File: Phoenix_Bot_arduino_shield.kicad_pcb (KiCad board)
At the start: 2 copper layers, 135.9 x 64.8 mm, 41 parts, among them J1 Analog_signal_male, J14 PWN(10-5), J15 On Board Supply, J16 1x8 Male, J17 1x8 Male, J18 PWM_(6-1), J19 Analog_Pin_1, J2 Encoder_Signal, J20 1x8 Female, J21 1x8 Female, J22 Serial, J23 ICSP, J24 Analog_Pin_2, J25 Digital_Pins, J27 Solenoid_terminal, J28 Solendoid_middle_terminal, J29 bottom_solenoid_terminal, J3 Servo_signal, J4 Analog_signal_female, J5 encoder_power, J6 Servo_ground, J7 encoder_ground, J8 12V_terminal, q1 solenoid_1, q2 solenoid_4, q3 solenoid_3, q4 solenoid_5, q5 solenoid_3, q6 solenoid_6

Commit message: Board design finished. Final review needed.
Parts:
- added G***: LOGO, ARC:arc-silk, F.Cu at (137.2, 105.4)
- added REF**: via-0.7mm, footprints:via-0.7mm, F.Cu at (245.1, 66.0)
- added REF**: via-0.7mm, footprints:via-0.7mm, F.Cu at (245.1, 123.8)
- added REF**: via-0.7mm, footprints:via-0.7mm, F.Cu at (236.2, 78.1)
- added REF**: via-0.7mm, footprints:via-0.7mm, F.Cu at (234.9, 78.1)
- added REF**: via-0.7mm, footprints:via-0.7mm, F.Cu at (246.4, 67.9)
- added REF**: via-0.7mm, footprints:via-0.7mm, F.Cu at (245.1, 67.9)
- added REF**: via-0.7mm, footprints:via-0.7mm, F.Cu at (243.8, 67.9)
- added REF**: via-0.7mm, footprints:via-0.7mm, F.Cu at (242.6, 67.9)
- added REF**: via-0.7mm, footprints:via-0.7mm, F.Cu at (241.3, 67.9)
- added REF**: via-0.7mm, footprints:via-0.7mm, F.Cu at (240.0, 67.9)
- added REF**: via-0.7mm, footprints:via-0.7mm, F.Cu at (238.8, 67.9)
- added REF**: via-0.7mm, footprints:via-0.7mm, F.Cu at (237.5, 67.9)
- added REF**: via-0.7mm, footprints:via-0.7mm, F.Cu at (246.4, 118.7)
- added REF**: via-0.7mm, footprints:via-0.7mm, F.Cu at (236.2, 67.9)
- added REF**: via-0.7mm, footprints:via-0.7mm, F.Cu at (234.9, 67.9)
- added REF**: via-0.7mm, footprints:via-0.7mm, F.Cu at (246.4, 64.1)
- added REF**: via-0.7mm, footprints:via-0.7mm, F.Cu at (245.1, 64.1)
- added REF**: via-0.7mm, footprints:via-0.7mm, F.Cu at (243.8, 64.1)
- added REF**: via-0.7mm, footprints:via-0.7mm, F.Cu at (242.6, 64.1)
- added REF**: via-0.7mm, footprints:via-0.7mm, F.Cu at (241.3, 64.1)
- added REF**: via-0.7mm, footprints:via-0.7mm, F.Cu at (240.0, 64.1)
- added REF**: via-0.7mm, footprints:via-0.7mm, F.Cu at (238.8, 64.1)
- added REF**: via-0.7mm, footprints:via-0.7mm, F.Cu at (237.5, 64.1)
- added REF**: via-0.7mm, footprints:via-0.7mm, F.Cu at (245.1, 118.7)
- added REF**: via-0.7mm, footprints:via-0.7mm, F.Cu at (236.2, 64.1)
- added REF**: via-0.7mm, footprints:via-0.7mm, F.Cu at (234.9, 64.1)
- added REF**: via-0.7mm, footprints:via-0.7mm, F.Cu at (246.4, 113.7)
- added REF**: via-0.7mm, footprints:via-0.7mm, F.Cu at (245.1, 113.7)
- added REF**: via-0.7mm, footprints:via-0.7mm, F.Cu at (246.4, 109.2)
- added REF**: via-0.7mm, footprints:via-0.7mm, F.Cu at (245.1, 109.2)
- added REF**: via-0.7mm, footprints:via-0.7mm, F.Cu at (246.4, 107.3)
- added REF**: via-0.7mm, footprints:via-0.7mm, F.Cu at (245.1, 107.3)
- added REF**: via-0.7mm, footprints:via-0.7mm, F.Cu at (245.1, 87.6)
- added REF**: via-0.7mm, footprints:via-0.7mm, F.Cu at (246.4, 66.0)
- added REF**: via-0.7mm, footprints:via-0.7mm, F.Cu at (246.4, 87.6)
- added REF**: via-0.7mm, footprints:via-0.7mm, F.Cu at (245.1, 85.7)
- added REF**: via-0.7mm, footprints:via-0.7mm, F.Cu at (246.4, 85.7)
- added REF**: via-0.7mm, footprints:via-0.7mm, F.Cu at (245.1, 81.9)
- added REF**: via-0.7mm, footprints:via-0.7mm, F.Cu at (246.4, 81.9)
- added REF**: via-0.7mm, footprints:via-0.7mm, F.Cu at (246.4, 83.8)
- added REF**: via-0.7mm, footprints:via-0.7mm, F.Cu at (245.1, 83.8)
- added REF**: via-0.7mm, footprints:via-0.7mm, F.Cu at (245.1, 80.0)
- added REF**: via-0.7mm, footprints:via-0.7mm, F.Cu at (246.4, 80.0)
- added REF**: via-0.7mm, footprints:via-0.7mm, F.Cu at (245.1, 103.5)
- added REF**: via-0.7mm, footprints:via-0.7mm, F.Cu at (245.1, 74.9)
- added REF**: via-0.7mm, footprints:via-0.7mm, F.Cu at (246.4, 103.5)
- added REF**: via-0.7mm, footprints:via-0.7mm, F.Cu at (245.1, 101.0)
- added REF**: via-0.7mm, footprints:via-0.7mm, F.Cu at (246.4, 101.0)
- added REF**: via-0.7mm, footprints:via-0.7mm, F.Cu at (245.1, 99.1)
- added REF**: via-0.7mm, footprints:via-0.7mm, F.Cu at (246.4, 99.1)
- added REF**: via-0.7mm, footprints:via-0.7mm, F.Cu at (245.1, 97.2)
- added REF**: via-0.7mm, footprints:via-0.7mm, F.Cu at (246.4, 97.2)
- added REF**: via-0.7mm, footprints:via-0.7mm, F.Cu at (245.1, 95.2)
- added REF**: via-0.7mm, footprints:via-0.7mm, F.Cu at (246.4, 95.2)
- added REF**: via-0.7mm, footprints:via-0.7mm, F.Cu at (245.1, 93.3)
- added REF**: via-0.7mm, footprints:via-0.7mm, F.Cu at (246.4, 74.9)
- added REF**: via-0.7mm, footprints:via-0.7mm, F.Cu at (246.4, 93.3)
- added REF**: via-0.7mm, footprints:via-0.7mm, F.Cu at (245.1, 91.4)
- added REF**: via-0.7mm, footprints:via-0.7mm, F.Cu at (246.4, 91.4)
- added REF**: via-0.7mm, footprints:via-0.7mm, F.Cu at (246.4, 121.9)
- added REF**: via-0.7mm, footprints:via-0.7mm, F.Cu at (245.1, 121.9)
- added REF**: via-0.7mm, footprints:via-0.7mm, F.Cu at (243.8, 121.9)
- added REF**: via-0.7mm, footprints:via-0.7mm, F.Cu at (242.6, 121.9)
- added REF**: via-0.7mm, footprints:via-0.7mm, F.Cu at (241.3, 121.9)
- added REF**: via-0.7mm, footprints:via-0.7mm, F.Cu at (240.0, 121.9)
- added REF**: via-0.7mm, footprints:via-0.7mm, F.Cu at (238.8, 121.9)
- added REF**: via-0.7mm, footprints:via-0.7mm, F.Cu at (245.1, 72.4)
- added REF**: via-0.7mm, footprints:via-0.7mm, F.Cu at (237.5, 121.9)
- added REF**: via-0.7mm, footprints:via-0.7mm, F.Cu at (236.2, 121.9)
- added REF**: via-0.7mm, footprints:via-0.7mm, F.Cu at (234.9, 121.9)
- added REF**: via-0.7mm, footprints:via-0.7mm, F.Cu at (246.4, 116.8)
- added REF**: via-0.7mm, footprints:via-0.7mm, F.Cu at (245.1, 116.8)
- added REF**: via-0.7mm, footprints:via-0.7mm, F.Cu at (243.8, 116.8)
- added REF**: via-0.7mm, footprints:via-0.7mm, F.Cu at (242.6, 116.8)
- added REF**: via-0.7mm, footprints:via-0.7mm, F.Cu at (241.3, 116.8)
- added REF**: via-0.7mm, footprints:via-0.7mm, F.Cu at (240.0, 116.8)
- added REF**: via-0.7mm, footprints:via-0.7mm, F.Cu at (238.8, 116.8)
- added REF**: via-0.7mm, footprints:via-0.7mm, F.Cu at (246.4, 72.4)
- added REF**: via-0.7mm, footprints:via-0.7mm, F.Cu at (237.5, 116.8)
- added REF**: via-0.7mm, footprints:via-0.7mm, F.Cu at (236.2, 116.8)
- added REF**: via-0.7mm, footprints:via-0.7mm, F.Cu at (246.4, 111.8)
- added REF**: via-0.7mm, footprints:via-0.7mm, F.Cu at (245.1, 111.8)
- added REF**: via-0.7mm, footprints:via-0.7mm, F.Cu at (243.8, 111.8)
- added REF**: via-0.7mm, footprints:via-0.7mm, F.Cu at (242.6, 111.8)
- added REF**: via-0.7mm, footprints:via-0.7mm, F.Cu at (241.3, 111.8)
- added REF**: via-0.7mm, footprints:via-0.7mm, F.Cu at (240.0, 111.8)
- added REF**: via-0.7mm, footprints:via-0.7mm, F.Cu at (238.8, 111.8)
- added REF**: via-0.7mm, footprints:via-0.7mm, F.Cu at (237.5, 111.8)
- added REF**: via-0.7mm, footprints:via-0.7mm, F.Cu at (245.1, 69.8)
- added REF**: via-0.7mm, footprints:via-0.7mm, F.Cu at (236.2, 111.8)
- added REF**: via-0.7mm, footprints:via-0.7mm, F.Cu at (234.9, 111.8)
- added REF**: via-0.7mm, footprints:via-0.7mm, F.Cu at (246.4, 105.4)
- added REF**: via-0.7mm, footprints:via-0.7mm, F.Cu at (245.1, 105.4)
- added REF**: via-0.7mm, footprints:via-0.7mm, F.Cu at (243.8, 105.4)
- added REF**: via-0.7mm, footprints:via-0.7mm, F.Cu at (242.6, 105.4)
- added REF**: via-0.7mm, footprints:via-0.7mm, F.Cu at (241.3, 105.4)
- added REF**: via-0.7mm, footprints:via-0.7mm, F.Cu at (240.0, 105.4)
- added REF**: via-0.7mm, footprints:via-0.7mm, F.Cu at (238.8, 105.4)
- added REF**: via-0.7mm, footprints:via-0.7mm, F.Cu at (237.5, 105.4)
- added REF**: via-0.7mm, footprints:via-0.7mm, F.Cu at (246.4, 69.8)
- added REF**: via-0.7mm, footprints:via-0.7mm, F.Cu at (236.2, 105.4)
- added REF**: via-0.7mm, footprints:via-0.7mm, F.Cu at (234.9, 105.4)
- added REF**: via-0.7mm, footprints:via-0.7mm, F.Cu at (246.4, 89.5)
- added REF**: via-0.7mm, footprints:via-0.7mm, F.Cu at (245.1, 89.5)
- added REF**: via-0.7mm, footprints:via-0.7mm, F.Cu at (243.8, 89.5)
- added REF**: via-0.7mm, footprints:via-0.7mm, F.Cu at (242.6, 89.5)
- added REF**: via-0.7mm, footprints:via-0.7mm, F.Cu at (241.3, 89.5)
- added REF**: via-0.7mm, footprints:via-0.7mm, F.Cu at (240.0, 89.5)
- added REF**: via-0.7mm, footprints:via-0.7mm, F.Cu at (238.8, 89.5)
- added REF**: via-0.7mm, footprints:via-0.7mm, F.Cu at (237.5, 89.5)
- added REF**: via-0.7mm, footprints:via-0.7mm, F.Cu at (246.4, 123.8)
- added REF**: via-0.7mm, footprints:via-0.7mm, F.Cu at (236.2, 89.5)
- added REF**: via-0.7mm, footprints:via-0.7mm, F.Cu at (234.9, 89.5)
- added REF**: via-0.7mm, footprints:via-0.7mm, F.Cu at (246.4, 78.1)
- added REF**: via-0.7mm, footprints:via-0.7mm, F.Cu at (245.1, 78.1)
- added REF**: via-0.7mm, footprints:via-0.7mm, F.Cu at (243.8, 78.1)
- added REF**: via-0.7mm, footprints:via-0.7mm, F.Cu at (242.6, 78.1)
- added REF**: via-0.7mm, footprints:via-0.7mm, F.Cu at (241.3, 78.1)
- added REF**: via-0.7mm, footprints:via-0.7mm, F.Cu at (240.0, 78.1)
- added REF**: via-0.7mm, footprints:via-0.7mm, F.Cu at (238.8, 78.1)
- added REF**: via-0.7mm, footprints:via-0.7mm, F.Cu at (237.5, 78.1)
- moved J8 4.62 mm to (115.6, 81.9), turned to 270 degrees
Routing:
- net /Ctrl_1: track 64.2 -> 43.0 mm
- net /Drain_2: track 50.3 -> 40.9 mm, vias 0 -> 3
- added copper zone on B.Cu, net +12V
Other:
- board text added: "12V"

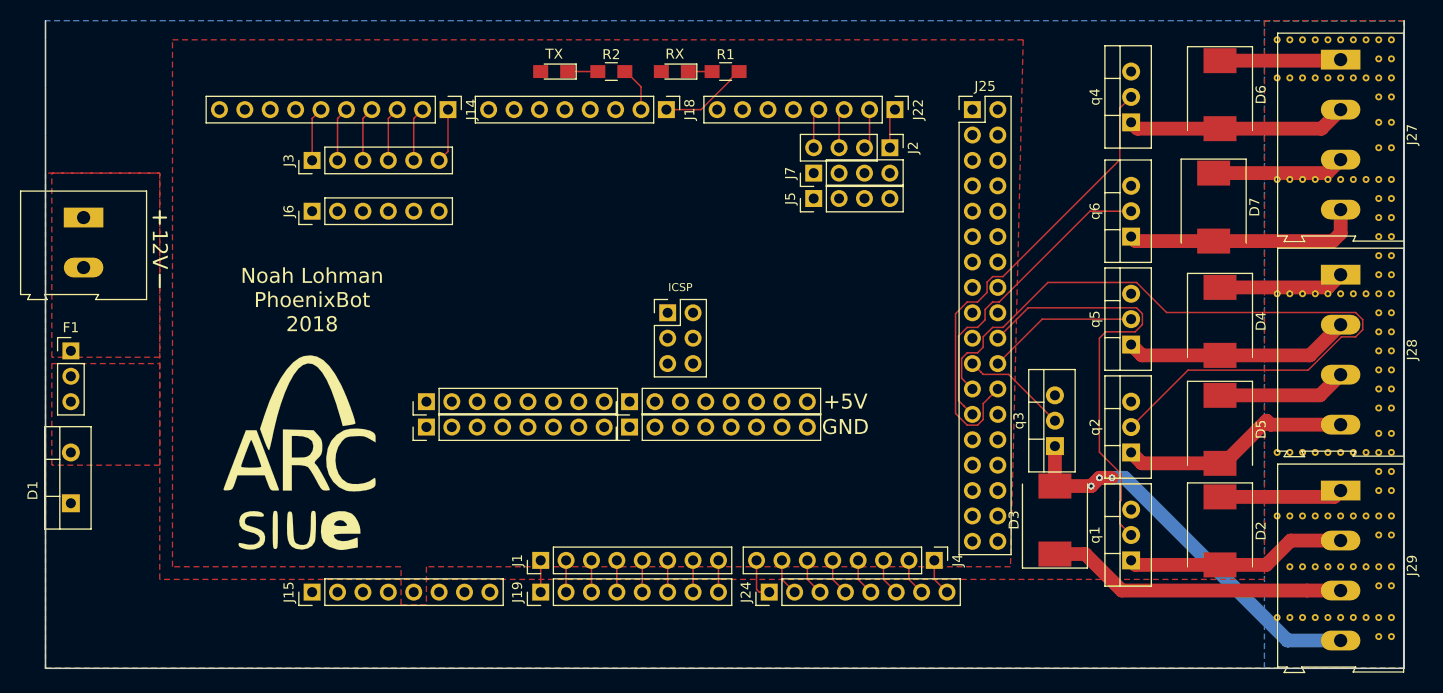
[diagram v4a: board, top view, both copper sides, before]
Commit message: Changed to 18 mil tracks for signals and 24 mil clearance to allow for easier etching.
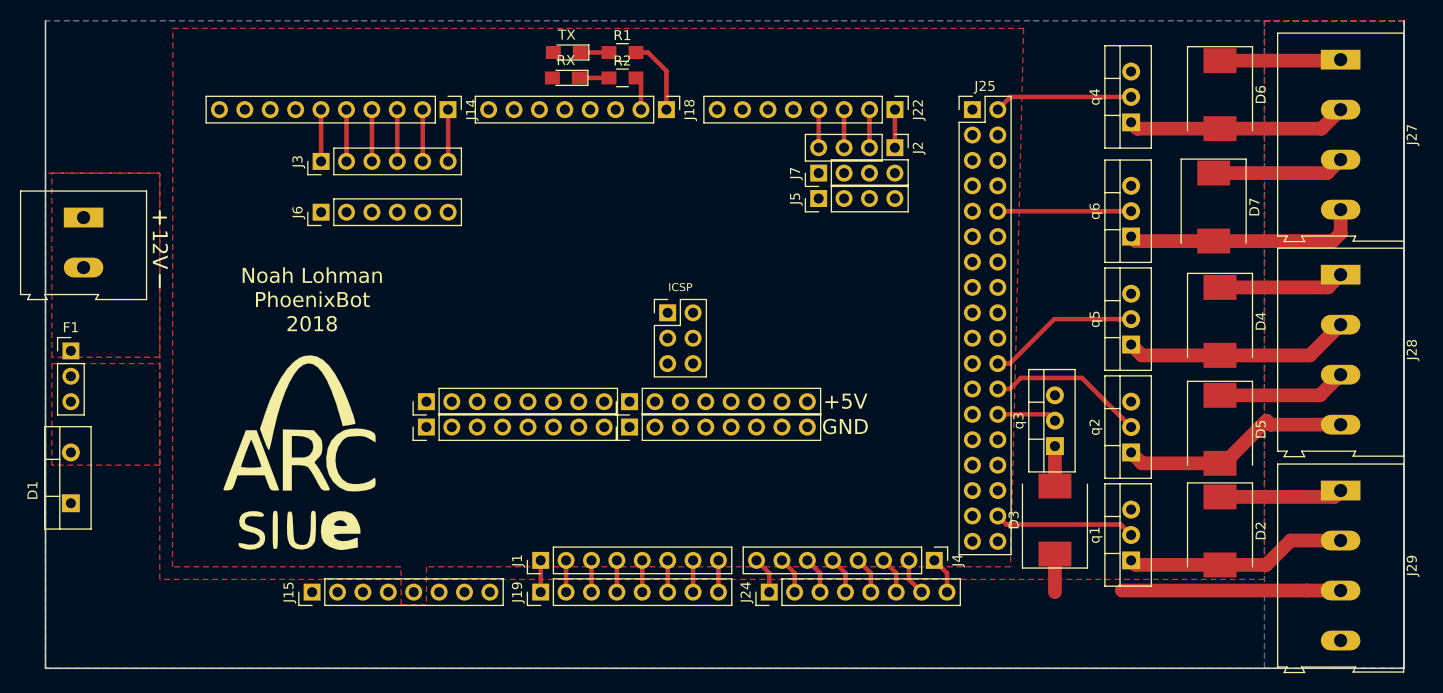
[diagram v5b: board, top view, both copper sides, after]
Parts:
- removed REF** (x121): via-0.7mm, footprints:via-0.7mm
- moved D8 10.9 mm to (163.8, 67.9)
- moved R1 10.5 mm to (169.5, 65.4)
- moved D9 2.29 mm to (163.9, 65.4)
- moved R2 1.28 mm to (169.5, 67.9)
- moved J3 0.91 mm to (139.3, 76.3)
- moved J6 0.91 mm to (139.3, 81.4)
- moved J2 0.50 mm to (196.7, 74.9)
- moved J5 0.50 mm to (189.1, 80.0)
- moved J7 0.50 mm to (189.1, 77.5)
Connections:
- J25 pad 10: Net-(J25-Pad10) -> /Ctrl_6
- J25 pad 2: Net-(J25-Pad2) -> /Ctrl_5
- J25 pad 20: /Ctrl_1 -> (no net)
- J25 pad 21: /Ctrl_2 -> (no net)
- J25 pad 23: /Ctrl_4 -> (no net)
- J25 pad 24: /Ctrl_5 -> /Ctrl_4
- J25 pad 25: /Ctrl_6 -> (no net)
- J25 pad 26: Net-(J25-Pad26) -> /Ctrl_2
- J25 pad 34: Net-(J25-Pad34) -> /Ctrl_1
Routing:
- net /Ctrl_4: track 77.1 -> 15.8 mm
- net /Drain_2: track 40.9 -> 3.99 mm, vias 3 -> 0
- net /Ctrl_5: track 47.3 -> 13.9 mm
- net /Ctrl_1: track 43.0 -> 14.1 mm
- net /Ctrl_6: track 31.4 -> 13.3 mm
- net /Ctrl_2: track 10.6 -> 5.98 mm
- net +12V: track 93.3 -> 88.8 mm
- net /TX: track 8.91 -> 7.68 mm
- net /RX: track 4.54 -> 3.39 mm
- net /Analog_9: track 4.29 -> 3.70 mm
- net Net-(D8-Pad1): track 2.38 -> 2.96 mm
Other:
- net class Default: clearance 0.1524 -> 0.6096; trace_width 0.1524 -> 0.4572
- rule trace_clearance: 0.1524 -> 0.6096
